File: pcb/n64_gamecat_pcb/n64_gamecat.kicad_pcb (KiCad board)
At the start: 2 copper layers, 120 x 163.8 mm, 4 parts

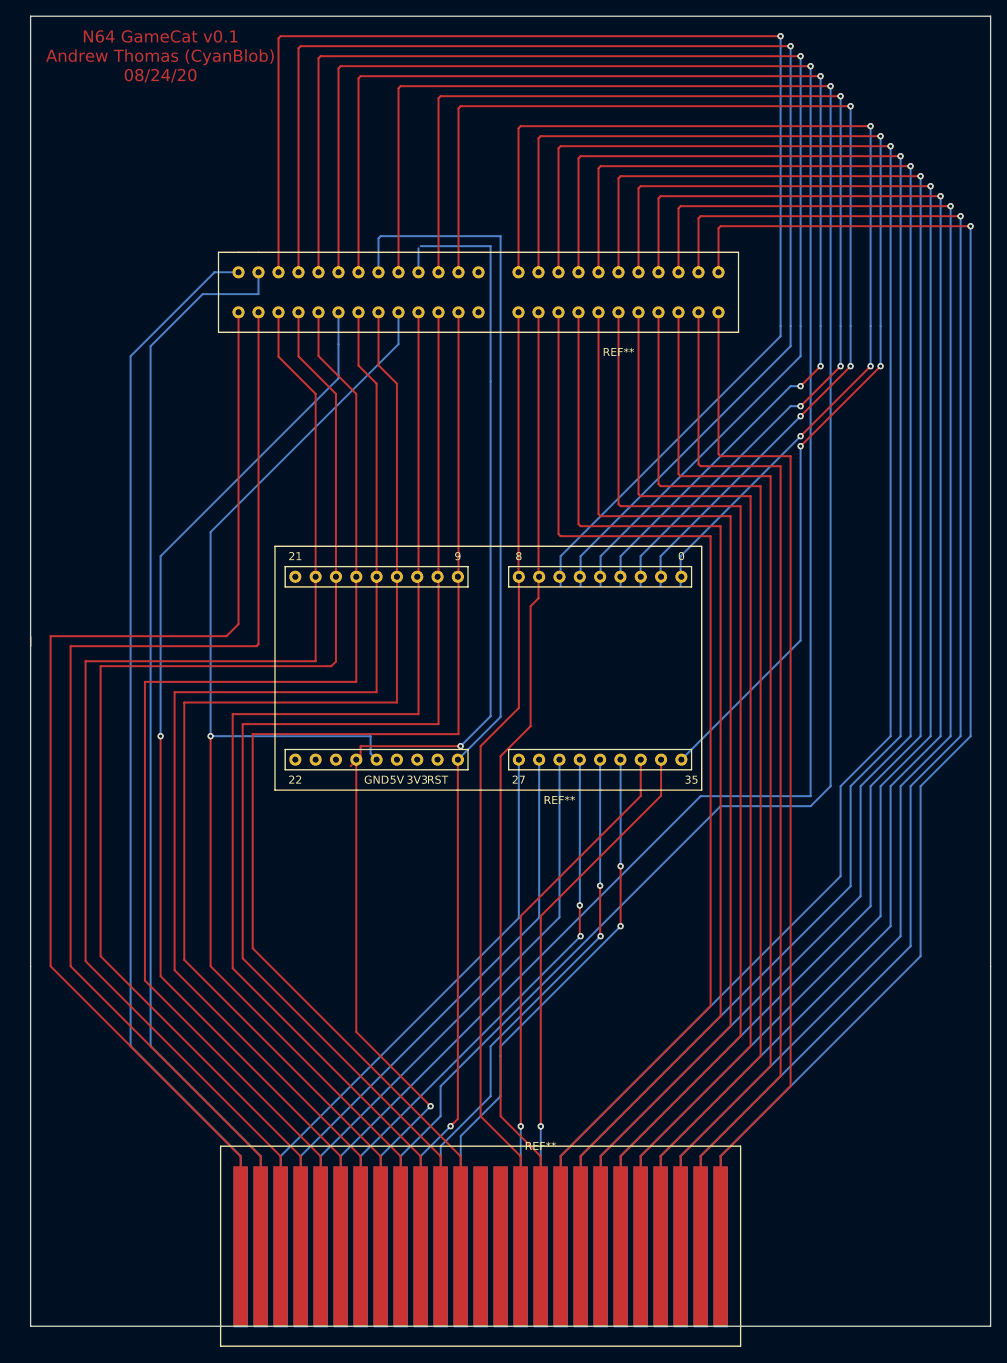
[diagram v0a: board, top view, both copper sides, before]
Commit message: Use pins other than 31-35, since they can't be used as GPIOHS
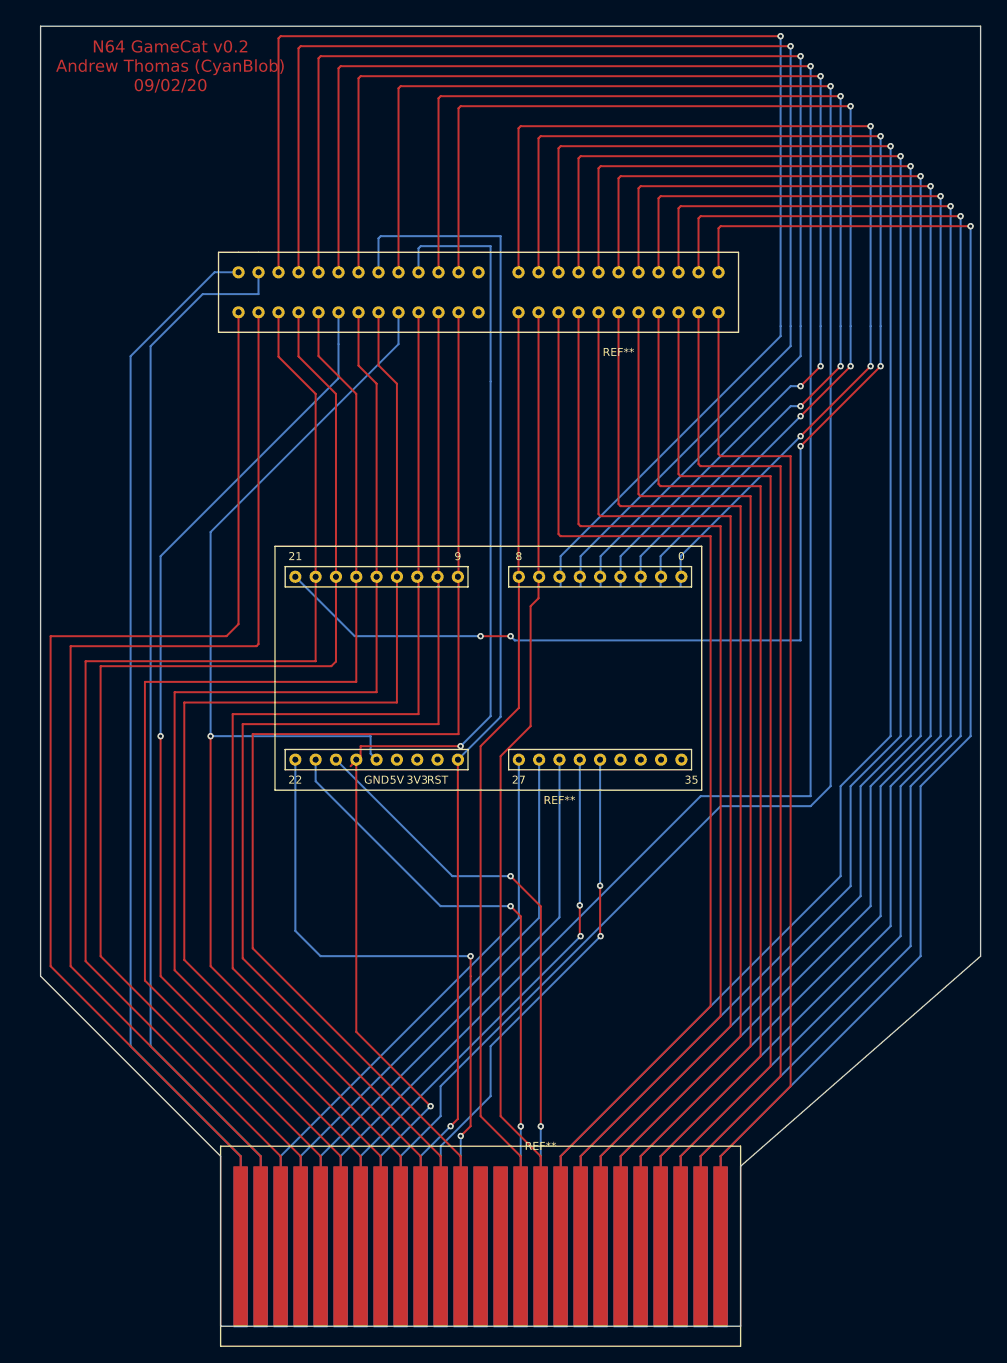
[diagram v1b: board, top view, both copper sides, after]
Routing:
- net (no net): track 7930.6 -> 8006.9 mm, vias 42 -> 46
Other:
- board size 120 x 163.8 mm -> 117.5 x 162.5 mm
- board text added: "N64 GameCat v0.2 Andrew Thomas (CyanBlob) 09/02/20"
- board text removed: "N64 GameCat v0.1 Andrew Thomas (CyanBlob) 08/24/20"

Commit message: Add rev 3 PCB
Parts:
- removed the REF** at (135.9, 109.2)
- added REF**: PinHeader_2x02_P2.54mm_Vertical, Connector_PinHeader_2.54mm:PinHeader_2x02_P2.54mm_Vertical, F.Cu at (144.8, 143.5)
- added REF**: PinHeader_2x02_P2.54mm_Vertical, Connector_PinHeader_2.54mm:PinHeader_2x02_P2.54mm_Vertical, F.Cu at (134.6, 143.5)
- added REF**: PinSocket_1x03_P2.54mm_Vertical, Connector_PinSocket_2.54mm:PinSocket_1x03_P2.54mm_Vertical, F.Cu at (114.3, 143.5)
- added REF**: PinSocket_1x03_P2.54mm_Vertical, Connector_PinSocket_2.54mm:PinSocket_1x03_P2.54mm_Vertical, F.Cu at (114.3, 147.3)
- added REF**: PinSocket_1x01_P2.54mm_Vertical, Connector_PinSocket_2.54mm:PinSocket_1x01_P2.54mm_Vertical, F.Cu at (124.5, 147.3)
- added REF**: PinSocket_1x01_P2.54mm_Vertical, Connector_PinSocket_2.54mm:PinSocket_1x01_P2.54mm_Vertical, F.Cu at (124.5, 143.5)
- added REF**: PinHeader_1x24_P2.54mm_Vertical, Connector_PinHeader_2.54mm:PinHeader_1x24_P2.54mm_Vertical, F.Cu at (161.3, 22.9)
- added REF**: PinHeader_1x24_P2.54mm_Vertical, Connector_PinHeader_2.54mm:PinHeader_1x24_P2.54mm_Vertical, F.Cu at (123.2, 22.9)
- moved REF** 10.5 mm to (135.9, 195.6)
- moved REF** 2.82 mm to (135.9, 147.3)
- turned REF** to 90 degrees
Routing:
- net (no net): track 8006.9 -> 6430.2 mm, vias 46 -> 67
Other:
- board text added: "N64 GameCat v0.3 Andrew Thomas (CyanBlob) 02/18/21"
- board text removed: "N64 GameCat v0.2 Andrew Thomas (CyanBlob) 09/02/20"
